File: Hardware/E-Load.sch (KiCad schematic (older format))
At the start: 8 parts, among them J1 Barrel_Jack, J2 Conn_01x05_Male, J3 Conn_01x08_Male, U1 AP2210K-3.3

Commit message: Replaced gate driver with opamp. Replaced feedback circuit with unity gain buffer
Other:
- moved on the sheet: FB1
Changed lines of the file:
@@
 L power:VDDA #PWR0111
 U 1 1 5F7DB02B
-P 6150 1150
-F 0 "#PWR0111" H 6150 1000 50  0001 C CNN
-F 1 "VDDA" H 6165 1323 50  0000 C CNN
-F 2 "" H 6150 1150 50  0001 C CNN
-F 3 "" H 6150 1150 50  0001 C CNN
-	1    6150 1150
+P 6550 2925
+F 0 "#PWR0111" H 6550 2775 50  0001 C CNN
+F 1 "VDDA" H 6565 3098 50  0000 C CNN
+F 2 "" H 6550 2925 50  0001 C CNN
+F 3 "" H 6550 2925 50  0001 C CNN
+	1    6550 2925
 	1    0    0    -1
 $EndComp
@@
 L power:+3V3 #PWR0112
 U 1 1 5F7DB56C
-P 5450 1150
-F 0 "#PWR0112" H 5450 1000 50  0001 C CNN
-F 1 "+3V3" H 5465 1323 50  0000 C CNN
-F 2 "" H 5450 1150 50  0001 C CNN
-F 3 "" H 5450 1150 50  0001 C CNN
-	1    5450 1150
+P 5850 2925
+F 0 "#PWR0112" H 5850 2775 50  0001 C CNN
+F 1 "+3V3" H 5865 3098 50  0000 C CNN
+F 2 "" H 5850 2925 50  0001 C CNN
+F 3 "" H 5850 2925 50  0001 C CNN
+	1    5850 2925
 	1    0    0    -1
 $EndComp
 Wire Wire Line
-	5450 1150 5450 1200
+	5850 2925 5850 2975
 Wire Wire Line
-	5450 1200 5650 1200
+	5850 2975 6050 2975
 Wire Wire Line
-	5950 1200 6150 1200
+	6350 2975 6550 2975
 Wire Wire Line
-	6150 1200 6150 1150
+	6550 2975 6550 2925
 $Sheet
 S 7275 4175 600  450
@@
 L Device:Ferrite_Bead FB1
 U 1 1 5F7DBADE
-P 5800 1200
-F 0 "FB1" V 6074 1200 50  0000 C CNN
-F 1 "Ferrite_Bead" V 5983 1200 50  0000 C CNN
-F 2 "Capacitor_SMD:C_1206_3216Metric" V 5730 1200 50  0001 C CNN
-F 3 "~" H 5800 1200 50  0001 C CNN
-	1    5800 1200
+P 6200 2975
+F 0 "FB1" V 6474 2975 50  0000 C CNN
+F 1 "Ferrite_Bead" V 6383 2975 50  0000 C CNN
+F 2 "Capacitor_SMD:C_1206_3216Metric" V 6130 2975 50  0001 C CNN
+F 3 "~" H 6200 2975 50  0001 C CNN
+	1    6200 2975
 	0    -1   -1   0
 $EndComp

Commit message: Added ADC instead of opamp. Added stiching
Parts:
- removed J1: Barrel_Jack, Connector_BarrelJack:BarrelJack_Wuerth_6941xx301002, symbol Connector:Barrel_Jack
- added J1: Barrel_Jack_Switch, Connector_BarrelJack:BarrelJack_Wuerth_6941xx301002, symbol Connector:Barrel_Jack_Switch
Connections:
- net +12V: now also J1.1
- net GND: now also J1.2, J1.3
- net MCU/SCL renamed CurrentControl/SCL
- net MCU/SDA renamed CurrentControl/SDA
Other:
- note added: "ADDR: 0111101"
- note added: "To SSD1306\nNOTE: will need to desolder \nvoltage translators on OLED"
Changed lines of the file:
@@
 F12 "BUTT_B" I L 5350 3650 50
 F13 "BUTT_C" I L 5350 3750 50
-F14 "PWM" I R 7000 4350 50
 $EndSheet
 Text Notes 10050 1100 0    50   ~ 0
 Requirements\n1. 12V DC input\n2. 0-10A Load current\n3. OLED Display\n4. 0- 30V load voltage\n5. 10mA increments\n
-$Comp
-L Connector:Barrel_Jack J1
-U 1 1 5F7B8D10
-P 1450 1200
-F 0 "J1" H 1507 1525 50  0000 C CNN
-F 1 "Barrel_Jack" H 1507 1434 50  0000 C CNN
-F 2 "Connector_BarrelJack:BarrelJack_Wuerth_6941xx301002" H 1500 1160 50  0001 C CNN
-F 3 "~" H 1500 1160 50  0001 C CNN
-	1    1450 1200
-	1    0    0    -1
-$EndComp
 $Comp
 L Device:C_Small C1
@@
 F1 "CurrentControl.sch" 50
 F2 "ADC" I L 7275 4425 50
-F3 "PWM" O L 7275 4350 50
+F3 "SCL" I L 7275 4250 50
+F4 "SDA" I L 7275 4325 50
 $EndSheet
 $Comp
@@
 $EndComp
 Wire Wire Line
-	7000 3950 9100 3950
-Wire Wire Line
-	7000 3850 9100 3850
+	7000 3950 7075 3950
+Wire Wire Line
+	7000 3850 7200 3850
 Wire Wire Line
 	7000 3750 7200 3750
@@
 Wire Wire Line
 	7275 4425 7000 4425
-Wire Wire Line
-	7275 4350 7000 4350
 $Comp
 L power:+12V #PWR0110
@@
 NoConn ~ 9100 3550
 NoConn ~ 9100 3750
+Wire Wire Line
+	7075 3950 7075 4325
+Wire Wire Line
+	7075 4325 7275 4325
+Connection ~ 7075 3950
+Wire Wire Line
+	7075 3950 9100 3950
+Wire Wire Line
+	7200 3850 7200 4250
+Wire Wire Line
+	7200 4250 7275 4250
+Connection ~ 7200 3850
+Wire Wire Line
+	7200 3850 9100 3850
+Text Notes 9050 4275 0    50   ~ 0
+ADDR: 0111101
+Text Notes 9050 4200 0    50   ~ 0
+To SSD1306\nNOTE: will need to desolder \nvoltage translators on OLED
+$Comp
+L Connector:Barrel_Jack_Switch J1
+U 1 1 5F8352CB
+P 1450 1200
+F 0 "J1" H 1507 1517 50  0000 C CNN
+F 1 "Barrel_Jack_Switch" H 1507 1426 50  0000 C CNN
+F 2 "Connector_BarrelJack:BarrelJack_Wuerth_6941xx301002" H 1500 1160 50  0001 C CNN
+F 3 "~" H 1500 1160 50  0001 C CNN
+	1    1450 1200
+	1    0    0    -1
+$EndComp
+Wire Wire Line
+	1750 1200 1750 1300
+Connection ~ 1750 1300
 $EndSCHEMATC

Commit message: Minor changes
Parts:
- J1: value Barrel_Jack_Switch -> PJ-002A
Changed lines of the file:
@@
 P 1450 1200
 F 0 "J1" H 1507 1517 50  0000 C CNN
-F 1 "Barrel_Jack_Switch" H 1507 1426 50  0000 C CNN
+F 1 "PJ-002A" H 1507 1426 50  0000 C CNN
 F 2 "Connector_BarrelJack:BarrelJack_Wuerth_6941xx301002" H 1500 1160 50  0001 C CNN
-F 3 "~" H 1500 1160 50  0001 C CNN
+F 3 "https://www.cuidevices.com/product/resource/pj-002a.pdf" H 1500 1160 50  0001 C CNN
 	1    1450 1200
 	1    0    0    -1

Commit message: updated C1 footprint, updated MCU schematic. Fixed possible issue with buttons
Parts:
- C1: footprint Capacitor_SMD:C_0603_1608Metric_Pad1.05x0.95mm_HandSolder -> Capacitor_THT:CP_Radial_D5.0mm_P2.50mm
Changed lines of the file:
@@
 encoding utf-8
 Sheet 1 4
-Title ""
-Date ""
-Rev ""
+Title "Electronic Load"
+Date "2020-10-12"
+Rev "0.0.1"
 Comp ""
 Comment1 ""
@@
 F 0 "C1" H 2342 1246 50  0000 L CNN
 F 1 "10u" H 2342 1155 50  0000 L CNN
-F 2 "Capacitor_SMD:C_0603_1608Metric_Pad1.05x0.95mm_HandSolder" H 2250 1200 50  0001 C CNN
+F 2 "Capacitor_THT:CP_Radial_D5.0mm_P2.50mm" H 2250 1200 50  0001 C CNN
 F 3 "~" H 2250 1200 50  0001 C CNN
 	1    2250 1200

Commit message: forgot to save
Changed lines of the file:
@@
 F7 "SCL" I R 7000 3850 50
 F8 "SDA" I R 7000 3950 50
-F9 "ADC" I R 7000 4425 50
-F10 "OLED_RST" I R 7000 3750 50
-F11 "BUTT_A" I L 5350 3550 50
-F12 "BUTT_B" I L 5350 3650 50
-F13 "BUTT_C" I L 5350 3750 50
+F9 "OLED_RST" I R 7000 3750 50
+F10 "BUTT_A" I L 5350 3550 50
+F11 "BUTT_B" I L 5350 3650 50
+F12 "BUTT_C" I L 5350 3750 50
+F13 "Vin_ADC" I R 7000 4475 50
+F14 "Currrent_ADC" I R 7000 4400 50
 $EndSheet
 Text Notes 10050 1100 0    50   ~ 0
@@
 F0 "CurrentControl" 50
 F1 "CurrentControl.sch" 50
-F2 "ADC" I L 7275 4425 50
-F3 "SCL" I L 7275 4250 50
-F4 "SDA" I L 7275 4325 50
+F2 "SCL" I L 7275 4250 50
+F3 "SDA" I L 7275 4325 50
+F4 "Vin_ADC" I L 7275 4475 50
+F5 "Current_ADC" I L 7275 4400 50
 $EndSheet
 $Comp
@@
 	0    -1   -1   0
 $EndComp
-Wire Wire Line
-	7275 4425 7000 4425
 $Comp
 L power:+12V #PWR0110
@@
 	1750 1200 1750 1300
 Connection ~ 1750 1300
+Wire Wire Line
+	7000 4475 7275 4475
+Wire Wire Line
+	7000 4400 7275 4400
 $EndSCHEMATC

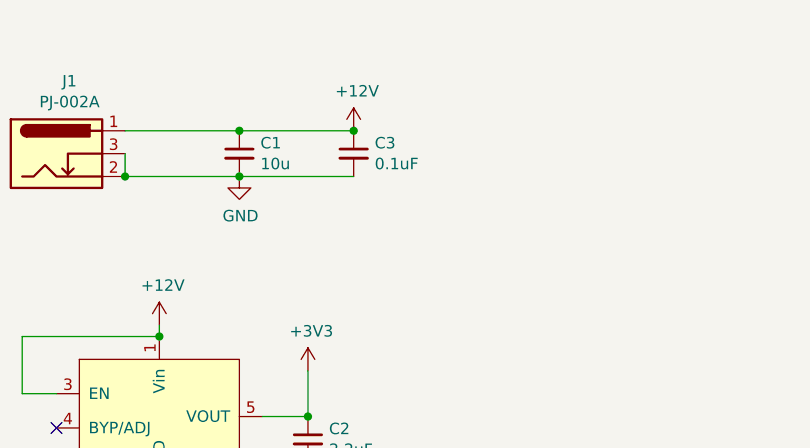
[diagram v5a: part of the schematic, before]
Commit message: Added LCSC part#, Thermal vias, etc
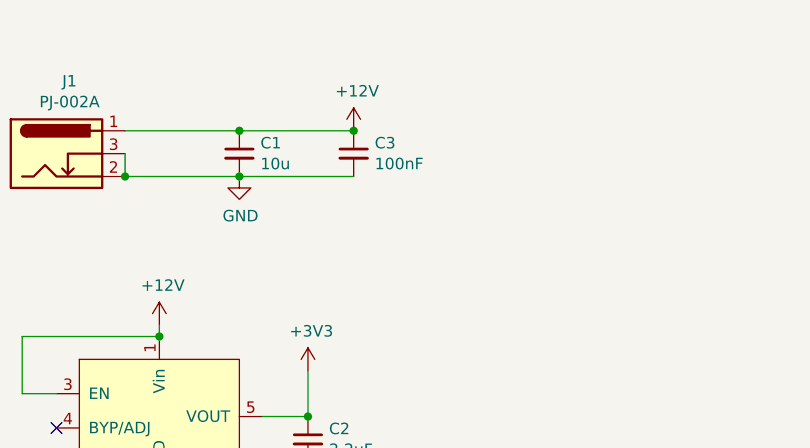
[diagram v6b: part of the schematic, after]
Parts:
- C1: DigiKey (none) -> 732-8937-1-ND; LCSC (none) -> C43799
- C2: LCSC (none) -> C92783
- C3: value 0.1uF -> 100nF; LCSC (none) -> C28061
- FB1: LCSC (none) -> C16902
- J1: Digikey (none) -> CP-002A-ND
- J2, J3: LCSC (none) -> C50981
- U1: LCSC (none) -> C264085
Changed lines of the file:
@@
 Requirements\n1. 12V DC input\n2. 0-10A Load current\n3. OLED Display\n4. 0- 30V load voltage\n5. 10mA increments\n
-$Comp
-L Device:C_Small C1
-U 1 1 5F7B9DE4
-P 2250 1200
-F 0 "C1" H 2342 1246 50  0000 L CNN
-F 1 "10u" H 2342 1155 50  0000 L CNN
-F 2 "Capacitor_THT:CP_Radial_D5.0mm_P2.50mm" H 2250 1200 50  0001 C CNN
-F 3 "~" H 2250 1200 50  0001 C CNN
-	1    2250 1200
-	1    0    0    -1
-$EndComp
 $Comp
 L Device:C_Small C3
@@
 P 2750 1200
 F 0 "C3" H 2842 1246 50  0000 L CNN
-F 1 "0.1uF" H 2842 1155 50  0000 L CNN
+F 1 "100nF" H 2842 1155 50  0000 L CNN
 F 2 "Capacitor_SMD:C_0603_1608Metric_Pad1.05x0.95mm_HandSolder" H 2750 1200 50  0001 C CNN
 F 3 "~" H 2750 1200 50  0001 C CNN
+F 4 "" H 2750 1200 50  0001 C CNN "Digikey"
+F 5 "C28061" H 2750 1200 50  0001 C CNN "LCSC"
 	1    2750 1200
 	1    0    0    -1
 $EndComp
-Wire Wire Line
-	1750 1100 2250 1100
-Connection ~ 2250 1100
-Wire Wire Line
-	2250 1100 2750 1100
 Wire Wire Line
 	1750 1300 2250 1300
@@
 F 2 "Package_TO_SOT_SMD:SOT-23-5_HandSoldering" H 1900 2350 50  0001 C CNN
 F 3 "" H 1900 2350 50  0001 C CNN
+F 4 "" H 1900 2350 50  0001 C CNN "Digikey"
+F 5 "C264085" H 1900 2350 50  0001 C CNN "LCSC"
 	1    1900 2350
 	1    0    0    -1
@@
 F 2 "Capacitor_SMD:C_0603_1608Metric_Pad1.05x0.95mm_HandSolder" H 2550 2450 50  0001 C CNN
 F 3 "~" H 2550 2450 50  0001 C CNN
+F 4 "" H 2550 2450 50  0001 C CNN "Digikey"
+F 5 "C92783" H 2550 2450 50  0001 C CNN "LCSC"
 	1    2550 2450
 	1    0    0    -1
@@
 F 2 "Connector_PinHeader_2.54mm:PinHeader_1x08_P2.54mm_Vertical" H 9300 3650 50  0001 C CNN
 F 3 "~" H 9300 3650 50  0001 C CNN
+F 4 "" H 9300 3650 50  0001 C CNN "Digikey"
+F 5 "C50981" H 9300 3650 50  0001 C CNN "LCSC"
 	1    9300 3650
 	-1   0    0    1
@@
 F 2 "Connector_PinHeader_2.54mm:PinHeader_1x05_P2.54mm_Vertical" H 7700 2250 50  0001 C CNN
 F 3 "~" H 7700 2250 50  0001 C CNN
+F 4 "" H 7700 2250 50  0001 C CNN "Digikey"
+F 5 "C50981" H 7700 2250 50  0001 C CNN "LCSC"
 	1    7700 2250
 	0    1    1    0
@@
 F 2 "Capacitor_SMD:C_1206_3216Metric" V 6130 2975 50  0001 C CNN
 F 3 "~" H 6200 2975 50  0001 C CNN
+F 4 "" V 6200 2975 50  0001 C CNN "Digikey"
+F 5 "C16902" V 6200 2975 50  0001 C CNN "LCSC"
 	1    6200 2975
 	0    -1   -1   0
@@
 F 2 "Connector_BarrelJack:BarrelJack_Wuerth_6941xx301002" H 1500 1160 50  0001 C CNN
 F 3 "https://www.cuidevices.com/product/resource/pj-002a.pdf" H 1500 1160 50  0001 C CNN
+F 4 "CP-002A-ND" H 1450 1200 50  0001 C CNN "Digikey"
 	1    1450 1200
 	1    0    0    -1
@@
 Wire Wire Line
 	7000 4400 7275 4400
+Wire Wire Line
+	2250 1100 2750 1100
+Wire Wire Line
+	1750 1100 2250 1100
+Connection ~ 2250 1100
+$Comp
+L Device:C_Small C1
+U 1 1 5F7B9DE4
+P 2250 1200
+F 0 "C1" H 2342 1246 50  0000 L CNN
+F 1 "10u" H 2342 1155 50  0000 L CNN
+F 2 "Capacitor_THT:CP_Radial_D5.0mm_P2.50mm" H 2250 1200 50  0001 C CNN
+F 3 "~" H 2250 1200 50  0001 C CNN
+F 4 "732-8937-1-ND" H 2250 1200 50  0001 C CNN "DigiKey"
+F 5 "C43799" H 2250 1200 50  0001 C CNN "LCSC"
+	1    2250 1200
+	1    0    0    -1
+$EndComp
 $EndSCHEMATC

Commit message: Added second mosfet and added FPaste layer on thermal vias
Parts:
- C1: DigiKey 732-8937-1-ND -> (none); Digikey (none) -> 732-8937-1-ND
- C3: LCSC C28061 -> C1591
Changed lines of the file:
@@
 F 3 "~" H 2750 1200 50  0001 C CNN
 F 4 "" H 2750 1200 50  0001 C CNN "Digikey"
-F 5 "C28061" H 2750 1200 50  0001 C CNN "LCSC"
+F 5 "C1591" H 2750 1200 50  0001 C CNN "LCSC"
 	1    2750 1200
 	1    0    0    -1
@@
 F 2 "Capacitor_THT:CP_Radial_D5.0mm_P2.50mm" H 2250 1200 50  0001 C CNN
 F 3 "~" H 2250 1200 50  0001 C CNN
-F 4 "732-8937-1-ND" H 2250 1200 50  0001 C CNN "DigiKey"
+F 4 "732-8937-1-ND" H 2250 1200 50  0001 C CNN "Digikey"
 F 5 "C43799" H 2250 1200 50  0001 C CNN "LCSC"
 	1    2250 1200
